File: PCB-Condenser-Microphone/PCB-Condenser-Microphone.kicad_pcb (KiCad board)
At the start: 2 copper layers, 16 x 38.1 mm, 22 parts, among them J1 Conn_01x02, J2 SJ-3523-SMT, SW1 SW_SPDT, U1 LM358

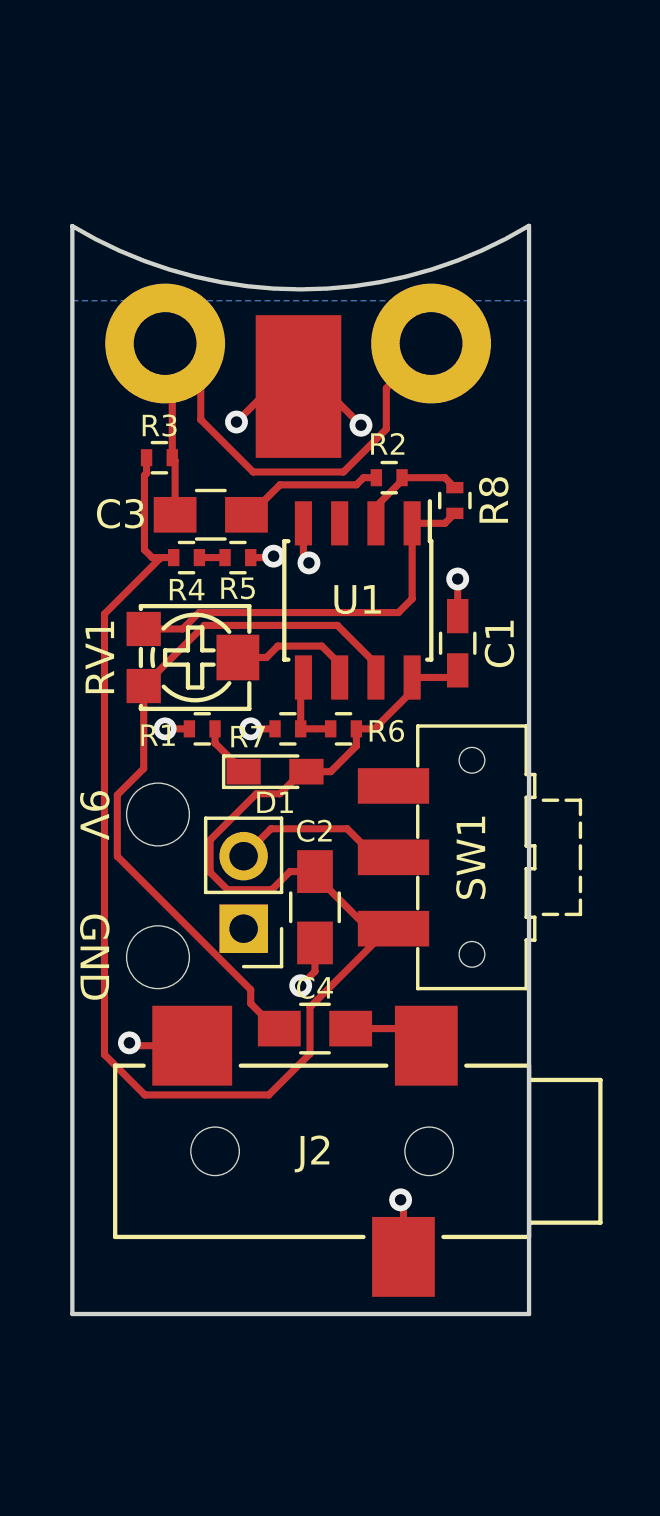
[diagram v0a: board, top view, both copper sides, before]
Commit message: Fixed an unconnected trace
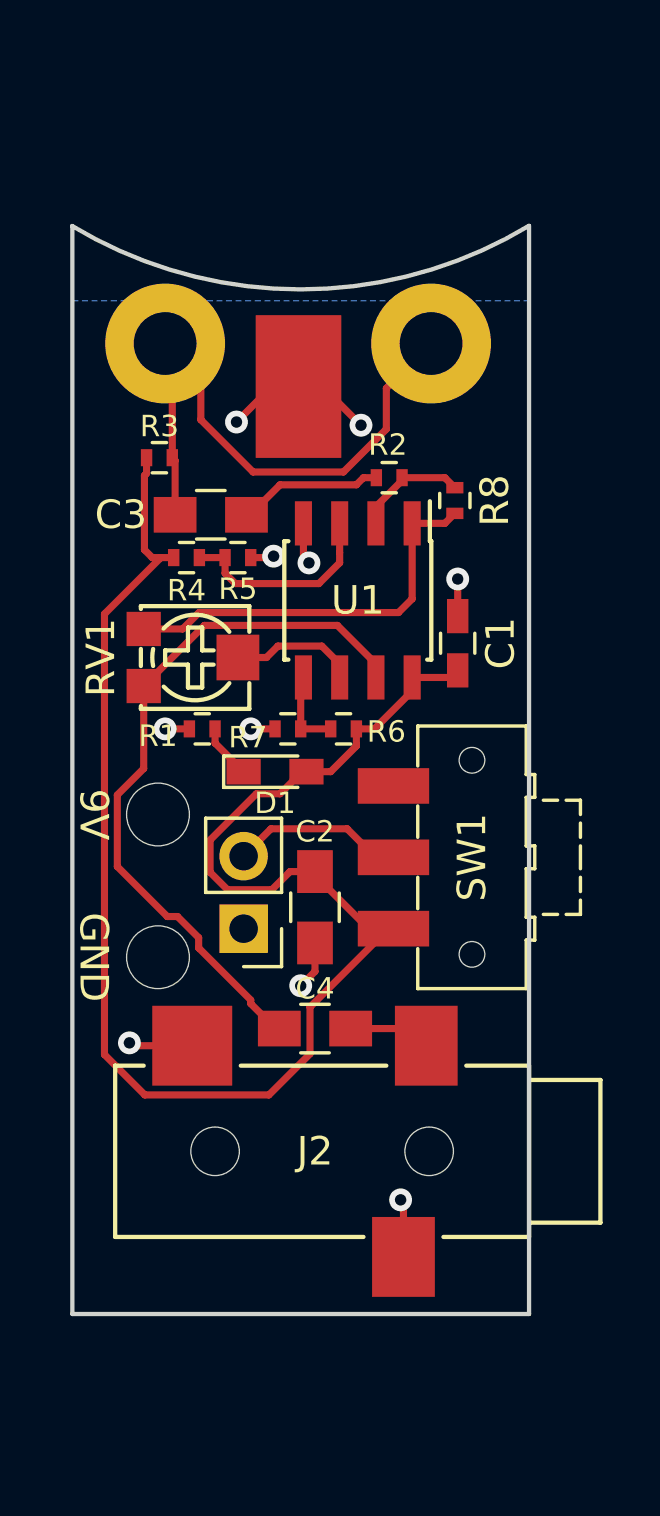
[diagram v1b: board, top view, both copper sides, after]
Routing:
- net Net-(R4-Pad2): track 0.90 -> 7.30 mm
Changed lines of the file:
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@@
     (thickness 1.6)
     (drawings 7)
-    (tracks 118)
+    (tracks 128)
     (zones 0)
     (modules 22)
@@
   )
   (layers
-    (0 F.Cu signal hide)
-    (31 B.Cu signal hide)
+    (0 F.Cu signal)
+    (31 B.Cu signal)
     (32 B.Adhes user)
     (33 F.Adhes user)
@@
   (segment (start 129.8 75) (end 130.4 75.6) (width 0.25) (layer F.Cu) (net 5))
   (segment (start 120.5 63) (end 120.5 65.890998) (width 0.25) (layer F.Cu) (net 6))
+  (segment (start 124.25 74.125) (end 125.125 75) (width 0.25) (layer F.Cu) (net 6))
   (segment (start 120.5 65.890998) (end 119.574999 66.815999) (width 0.25) (layer F.Cu) (net 6))
-  (segment (start 119.574999 66.815999) (end 119.574999 68.965997) (width 0.25) (layer F.Cu) (net 6))
-  (segment (start 119.574999 68.965997) (end 124.25 73.640998) (width 0.25) (layer F.Cu) (net 6))
-  (segment (start 124.25 73.640998) (end 124.25 74.125) (width 0.25) (layer F.Cu) (net 6))
-  (segment (start 124.25 74.125) (end 125.125 75) (width 0.25) (layer F.Cu) (net 6))
+  (segment (start 122.425001 71.815999) (end 122.425001 72.175001) (width 0.25) (layer F.Cu) (net 6))
+  (segment (start 119.574999 66.815999) (end 119.574999 69.324999) (width 0.25) (layer F.Cu) (net 6))
+  (segment (start 119.574999 69.324999) (end 121.324999 71.074999) (width 0.25) (layer F.Cu) (net 6))
+  (segment (start 121.324999 71.074999) (end 121.684001 71.074999) (width 0.25) (layer F.Cu) (net 6))
+  (segment (start 124.25 74) (end 124.25 74.125) (width 0.25) (layer F.Cu) (net 6))
   (segment (start 125.125 75) (end 125.25 75) (width 0.25) (layer F.Cu) (net 6))
+  (segment (start 121.684001 71.074999) (end 122.425001 71.815999) (width 0.25) (layer F.Cu) (net 6))
+  (segment (start 122.425001 72.175001) (end 124.25 74) (width 0.25) (layer F.Cu) (net 6))
   (segment (start 128.635 62.7) (end 128.635 62.225) (width 0.25) (layer F.Cu) (net 6))
   (segment (start 128.635 62.225) (end 127.284999 60.874999) (width 0.25) (layer F.Cu) (net 6))
@@
   (segment (start 129.55 55.8) (end 129.55 55.7) (width 0.25) (layer F.Cu) (net 9))
   (segment (start 128.635 56.715) (end 129.55 55.8) (width 0.25) (layer F.Cu) (net 9))
+  (segment (start 123.35 58.5) (end 123.35 59.05) (width 0.25) (layer F.Cu) (net 10))
+  (segment (start 123.35 59.05) (end 123.710796 59.410796) (width 0.25) (layer F.Cu) (net 10))
+  (segment (start 123.710796 59.410796) (end 126.6369 59.410796) (width 0.25) (layer F.Cu) (net 10))
+  (segment (start 126.6369 59.410796) (end 127.365 58.682696) (width 0.25) (layer F.Cu) (net 10))
+  (segment (start 127.365 58.682696) (end 127.365 58.325) (width 0.25) (layer F.Cu) (net 10))
+  (segment (start 127.365 58.325) (end 127.365 57.3) (width 0.25) (layer F.Cu) (net 10))
   (segment (start 122.45 58.5) (end 123.35 58.5) (width 0.25) (layer F.Cu) (net 10))
   (segment (start 126 64.5) (end 126 62.795) (width 0.25) (layer F.Cu) (net 11))

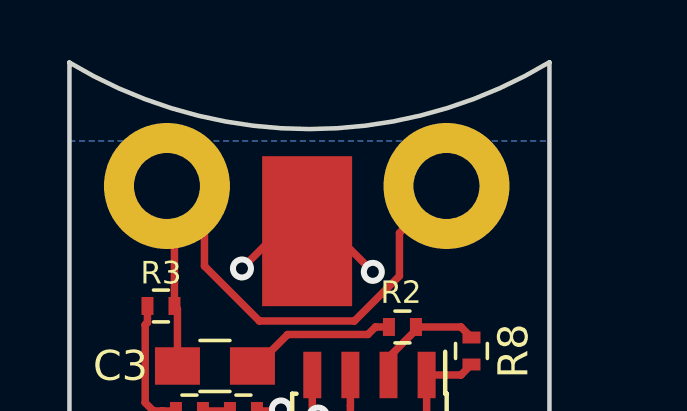
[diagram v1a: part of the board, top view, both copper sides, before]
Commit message: Fixed pcb outline and regenerated gerber
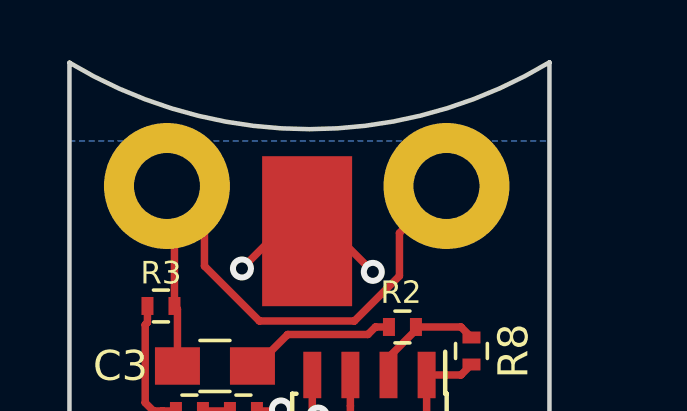
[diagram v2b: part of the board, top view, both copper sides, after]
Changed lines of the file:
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@@
   (gr_line (start 118 85) (end 118 46.89) (layer Edge.Cuts) (width 0.15))
   (gr_line (start 134 85) (end 134 46.88) (layer Edge.Cuts) (width 0.15))
-  (gr_arc (start 125.99 33.6) (end 117.990001 46.879999) (angle -62.16197563) (layer Edge.Cuts) (width 0.15))
+  (gr_arc (start 125.99 33.6) (end 118 46.89) (angle -62.11124932) (layer Edge.Cuts) (width 0.15))
   (gr_line (start 118 85) (end 134 85) (layer Edge.Cuts) (width 0.15))
   (segment (start 120.524999 58.224999) (end 120.8 58.5) (width 0.25) (layer F.Cu) (net 1))

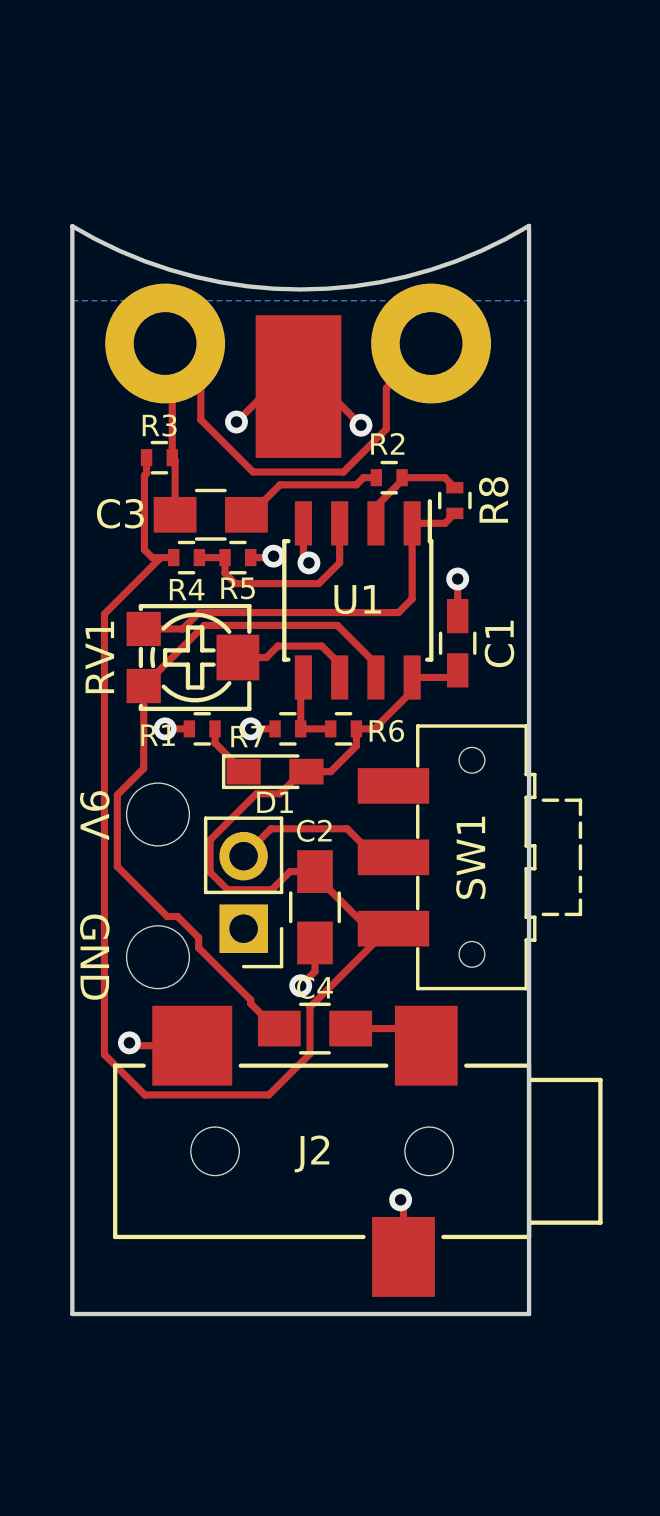
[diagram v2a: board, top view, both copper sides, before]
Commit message: Updated circuit to match the jfet
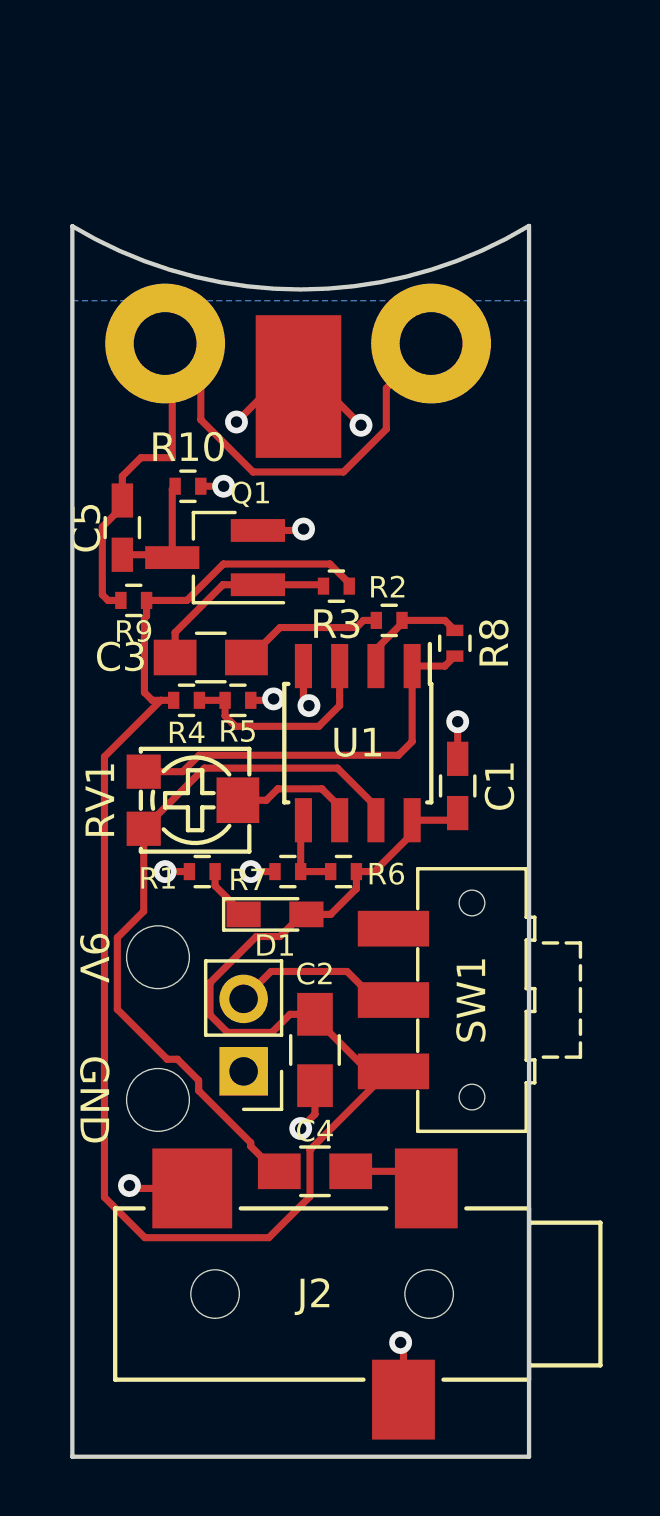
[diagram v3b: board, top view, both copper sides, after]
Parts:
- removed REF***: OSHW-Logo_5.7x6mm_SilkScreen, Symbols:OSHW-Logo_5.7x6mm_SilkScreen
- added C5: 680pF, Capacitors_SMD:C_0603_HandSoldering, F.Cu at (119.8, 57.5)
- added Q1: Q_NJFET_DSG, TO_SOT_Packages_SMD:SOT-23_Handsoldering, F.Cu at (123.0, 58.5)
- added R10: 100M, Resistors_SMD:R_0402, F.Cu at (122.0, 56.0)
- added R9: 100M, Resistors_SMD:R_0402, F.Cu at (120.2, 60.0)
- R3: value 10k -> 300
- moved R3 7.66 mm to (127.2, 59.5), turned to 180 degrees
- moved C1 5.00 mm to (131.5, 66.5)
- moved C2 5.00 mm to (126.5, 75.8)
- moved C3 5.00 mm to (122.8, 62.0)
- moved C4 5.00 mm to (126.5, 80.0)
- moved D1 5.00 mm to (125.1, 71.0)
- moved J1 5.00 mm to (124.0, 76.5)
- moved J2 5.00 mm to (126.5, 84.3)
- moved MT1 5.00 mm to (121.0, 72.5)
- moved MT2 5.00 mm to (121.0, 77.5)
- moved R1 5.00 mm to (122.5, 69.5)
- moved R2 5.00 mm to (129.1, 60.7)
- moved R4 5.00 mm to (122.0, 63.5)
- moved R5 5.00 mm to (123.8, 63.5)
- moved R6 5.00 mm to (127.5, 69.5)
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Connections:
- MK1 pad 2: Net-(C3-Pad2) -> Net-(C5-Pad2)
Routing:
- net Net-(C5-Pad2): track 0.00 -> 26.0 mm
- net Net-(C3-Pad2): track 20.9 -> 6.79 mm
- net +9V: track 57.4 -> 65.5 mm
- net Net-(C5-Pad1): track 0.00 -> 4.33 mm
- net GND: track 16.7 -> 19.1 mm, vias 10 -> 12
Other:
- board size 16 x 38.1 mm -> 16 x 43.1 mm

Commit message: Uodated JFET
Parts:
- R3: value 300 -> 10K

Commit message: Added back OSHW logo to preamp
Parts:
- added REF***: OSHW-Logo2_7.3x6mm_SilkScreen, Symbols:OSHW-Logo2_7.3x6mm_SilkScreen, B.Cu at (121.8, 58.6)

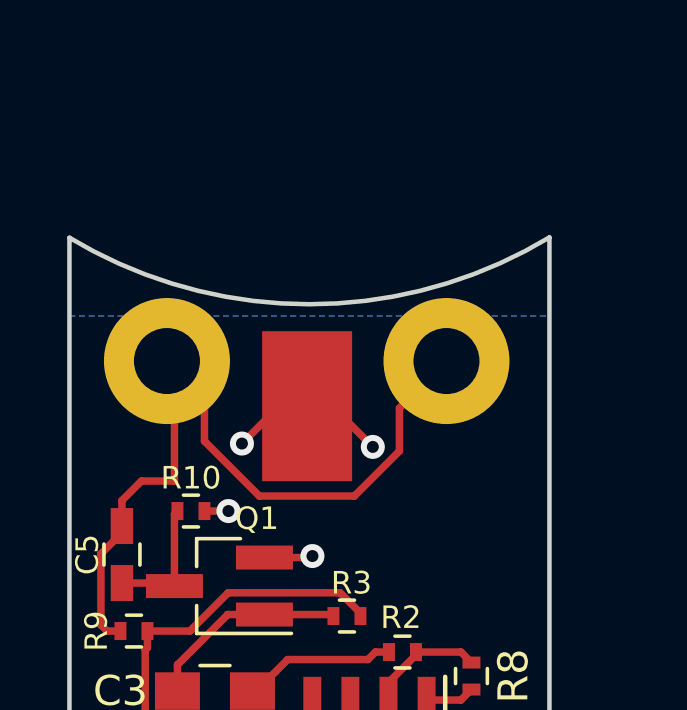
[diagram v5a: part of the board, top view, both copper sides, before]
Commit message: Switched ground and bias on microphone preamp
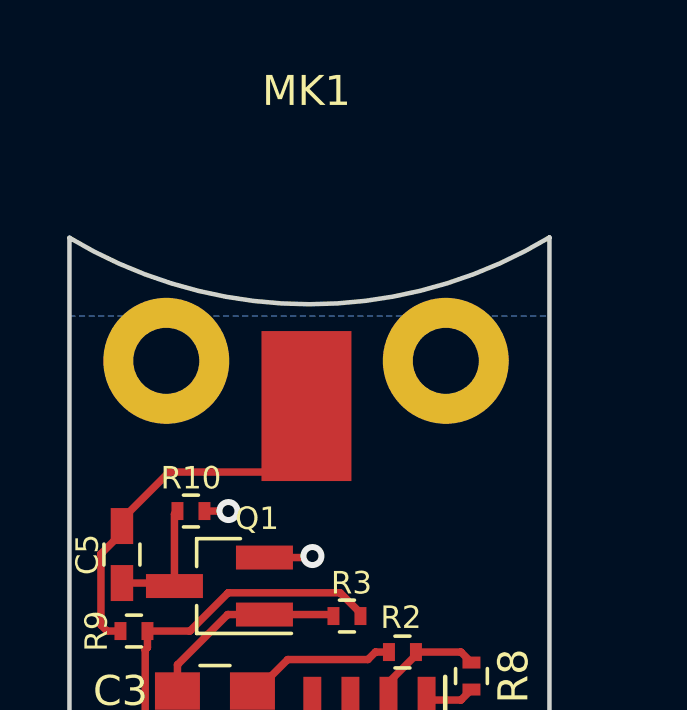
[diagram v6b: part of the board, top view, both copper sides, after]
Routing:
- net Net-(C5-Pad2): track 26.0 -> 12.8 mm
- net GND: track 19.1 -> 13.7 mm, vias 12 -> 10
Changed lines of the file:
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@@
     (thickness 1.6)
     (drawings 7)
-    (tracks 154)
+    (tracks 141)
     (zones 0)
     (modules 26)
@@
     (last_trace_width 0.25)
     (trace_clearance 0.2)
-    (zone_clearance 0.508)
+    (zone_clearance 0.5)
     (zone_45_only no)
     (trace_min 0.2)
@@
       (rotate (xyz 0 0 0))
     )
-  )
-  (module PCB-Condenser-Microphone:Condenser-Microphone-Backplate-30mm-Single-mount (layer F.Cu)
-    (at 125.922463 51.007055)
-    (fp_text reference MK1 (at 0 -9) (layer F.SilkS) hide
-      (effects (font (size 1 1) (thickness 0.15)))
-    )
-    (fp_text value Microphone_Condenser (at 0 9) (layer F.Fab)
-      (effects (font (size 1 1) (thickness 0.15)))
-    )
-    (pad 2 thru_hole circle (at 4.645023 -0.007055 285) (size 4.2 4.2) (drill 2.2) (layers *.Cu *.Mask)
-      (net 11 "Net-(C5-Pad2)") (clearance 1))
-    (pad 2 thru_hole circle (at -4.672463 -0.007055 255) (size 4.2 4.2) (drill 2.2) (layers *.Cu *.Mask)
-      (net 11 "Net-(C5-Pad2)") (clearance 1))
-    (pad 1 smd rect (at 0 1.5) (size 3 5) (layers F.Cu F.Paste F.Mask)
-      (net 2 GND))
   )
   (module Capacitors_SMD:C_0603_HandSoldering (layer F.Cu)
@@
       (xy -0.113933 2.757629) (xy -0.013056 2.757714) (xy 0 2.757714) (xy 0.10391 2.757652)) (layer B.SilkS) (width 0.01))
   )
+  (module PCB-Condenser-Microphone:Condenser-Microphone-Backplate-30mm-Single-mount (layer F.Cu)
+    (at 125.9 51)
+    (fp_text reference MK1 (at 0 -9) (layer F.SilkS)
+      (effects (font (size 1 1) (thickness 0.15)))
+    )
+    (fp_text value Microphone_Condenser (at 0 9) (layer F.Fab)
+      (effects (font (size 1 1) (thickness 0.15)))
+    )
+    (pad 1 thru_hole circle (at 4.645023 -0.007055 285) (size 4.2 4.2) (drill 2.2) (layers *.Cu *.Mask)
+      (net 2 GND) (clearance 1))
+    (pad 1 thru_hole circle (at -4.672463 -0.007055 255) (size 4.2 4.2) (drill 2.2) (layers *.Cu *.Mask)
+      (net 2 GND) (clearance 1))
+    (pad 2 smd rect (at 0 1.5) (size 3 5) (layers F.Cu F.Paste F.Mask)
+      (net 11 "Net-(C5-Pad2)"))
+  )
   (gr_text 9V (at 118.75 72.5 270) (layer F.SilkS)
     (effects (font (size 1 1) (thickness 0.15)))
@@
   (segment (start 131.5 65.55) (end 131.5 64.25) (width 0.25) (layer F.Cu) (net 2) (status 10))
   (via (at 131.5 64.25) (size 0.8) (drill 0.4) (layers F.Cu B.Cu) (net 2))
-  (via (at 123.75 53.75) (size 0.8) (drill 0.4) (layers F.Cu B.Cu) (net 2))
-  (segment (start 123.75 53.75) (end 124.992945 52.507055) (width 0.25) (layer F.Cu) (net 2) (status 20))
-  (segment (start 124.992945 52.507055) (end 125.922463 52.507055) (width 0.25) (layer F.Cu) (net 2) (status 30))
-  (segment (start 125.922463 52.507055) (end 126.757055 52.507055) (width 0.25) (layer F.Cu) (net 2) (status 30))
-  (segment (start 126.757055 52.507055) (end 128.112347 53.862347) (width 0.25) (layer F.Cu) (net 2) (status 10))
-  (via (at 128.112347 53.862347) (size 0.8) (drill 0.4) (layers F.Cu B.Cu) (net 2))
   (segment (start 126.095 62.3) (end 126.095 63.491896) (width 0.25) (layer F.Cu) (net 2) (status 10))
   (segment (start 126.095 63.491896) (end 126.288899 63.685795) (width 0.25) (layer F.Cu) (net 2))
@@
   (segment (start 124.5 59.45) (end 126.75 59.45) (width 0.25) (layer F.Cu) (net 3) (status 30))
   (segment (start 126.75 59.45) (end 126.8 59.5) (width 0.25) (layer F.Cu) (net 3) (status 30))
-  (segment (start 119.75 56.5) (end 119.75 55.65) (width 0.25) (layer F.Cu) (net 11) (status 10))
-  (segment (start 119.75 55.65) (end 120.4 55) (width 0.25) (layer F.Cu) (net 11))
-  (segment (start 120.4 55) (end 121.5 55) (width 0.25) (layer F.Cu) (net 11))
+  (segment (start 119.75 56.5) (end 119.75 56.275) (width 0.25) (layer F.Cu) (net 11))
+  (segment (start 119.75 56.275) (end 121.325 54.7) (width 0.25) (layer F.Cu) (net 11))
+  (segment (start 121.325 54.7) (end 124.7 54.7) (width 0.25) (layer F.Cu) (net 11))
+  (segment (start 124.7 54.7) (end 125.9 53.5) (width 0.25) (layer F.Cu) (net 11))
+  (segment (start 125.9 53.5) (end 125.9 52.5) (width 0.25) (layer F.Cu) (net 11))
   (segment (start 119.7 60) (end 119.25 60) (width 0.25) (layer F.Cu) (net 11) (status 10))
   (segment (start 119.25 60) (end 119.049999 59.799999) (width 0.25) (layer F.Cu) (net 11))
@@
   (segment (start 119.049999 57.425001) (end 119.75 56.725) (width 0.25) (layer F.Cu) (net 11) (status 20))
   (segment (start 119.75 56.725) (end 119.75 56.5) (width 0.25) (layer F.Cu) (net 11) (status 30))
-  (segment (start 121.25 51) (end 122.5 52.25) (width 0.25) (layer F.Cu) (net 11) (status 30))
-  (segment (start 122.5 53.669594) (end 124.330406 55.5) (width 0.25) (layer F.Cu) (net 11))
-  (segment (start 127.5 55.5) (end 129 54) (width 0.25) (layer F.Cu) (net 11))
-  (segment (start 122.5 52.25) (end 122.5 53.669594) (width 0.25) (layer F.Cu) (net 11) (status 10))
-  (segment (start 124.330406 55.5) (end 127.5 55.5) (width 0.25) (layer F.Cu) (net 11))
-  (segment (start 129 54) (end 129 52.567486) (width 0.25) (layer F.Cu) (net 11))
-  (segment (start 129 52.567486) (end 130.567486 51) (width 0.25) (layer F.Cu) (net 11) (status 20))
-  (segment (start 121.5 55) (end 121.5 51.25) (width 0.25) (layer F.Cu) (net 11) (status 20))
-  (segment (start 121.5 51.25) (end 121.25 51) (width 0.25) (layer F.Cu) (net 11) (status 30))
   (segment (start 124.1 62) (end 124.225 62) (width 0.25) (layer F.Cu) (net 4) (status 30))
   (segment (start 124.225 62) (end 125.27499 60.95001) (width 0.25) (layer F.Cu) (net 4) (status 10))
@@
   (segment (start 127.365 67.225) (end 127.365 67.7) (width 0.25) (layer F.Cu) (net 10) (status 30))
   (zone (net 2) (net_name GND) (layer B.Cu) (hatch edge 0.508)
-    (connect_pads (clearance 0.5))
+    (connect_pads yes (clearance 0.5))
     (min_thickness 0.254)
-    (fill yes (arc_segments 16) (thermal_gap 0.5) (thermal_bridge_width 0.5))
+    (fill yes (arc_segments 16) (thermal_gap 0.5) (thermal_bridge_width 1))
     (polygon
       (pts
